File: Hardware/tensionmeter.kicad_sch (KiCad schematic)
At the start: 28 parts, among them IC2 MCP1501T-18E_CHY, U15 L7812, U16 MCP6002-xSN, U24 AD8226BRMZ-R7, U25 AD8226BRMZ-R7

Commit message: Fused 12V
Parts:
- added F7: 300mA, Fuse:Fuse_0603_1608Metric_Pad1.05x0.95mm_HandSolder, symbol Device:Polyfuse_Small
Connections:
- net +12V: now also F7.2; no longer C72.1, U15.3 (OUT)
- new net: C72.1, F7.1, U15.3 (OUT)
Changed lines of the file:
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@@
 	(wire
 		(pts
-			(xy 247.65 64.77) (xy 247.65 67.31)
-		)
-		(stroke
-			(width 0)
-			(type default)
-		)
-	)
-	(wire
-		(pts
 			(xy 114.3 111.76) (xy 132.08 111.76)
 		)
@@
 	(wire
 		(pts
+			(xy 255.27 62.23) (xy 255.27 67.31)
+		)
+		(stroke
+			(width 0)
+			(type default)
+		)
+	)
+	(wire
+		(pts
 			(xy 46.99 96.52) (xy 49.53 96.52)
 		)
@@
 	(wire
 		(pts
+			(xy 255.27 67.31) (xy 251.46 67.31)
+		)
+		(stroke
+			(width 0)
+			(type default)
+		)
+	)
+	(wire
+		(pts
 			(xy 91.44 52.07) (xy 104.14 52.07)
 		)
@@
 	(wire
 		(pts
-			(xy 233.68 77.47) (xy 233.68 74.93)
+			(xy 243.84 67.31) (xy 246.38 67.31)
 		)
 		(stroke
@@
 	(wire
 		(pts
-			(xy 67.31 62.23) (xy 67.31 66.04)
+			(xy 233.68 77.47) (xy 233.68 74.93)
 		)
 		(stroke
@@
 	(wire
 		(pts
-			(xy 142.24 54.61) (xy 163.83 54.61)
+			(xy 67.31 62.23) (xy 67.31 66.04)
 		)
 		(stroke
@@
 	(wire
 		(pts
-			(xy 132.08 101.6) (xy 142.24 101.6)
+			(xy 142.24 54.61) (xy 163.83 54.61)
 		)
 		(stroke
@@
 	(wire
 		(pts
-			(xy 214.63 64.77) (xy 214.63 67.31)
+			(xy 132.08 101.6) (xy 142.24 101.6)
 		)
 		(stroke
@@
 	(wire
 		(pts
-			(xy 31.75 87.63) (xy 31.75 88.9)
+			(xy 214.63 64.77) (xy 214.63 67.31)
 		)
 		(stroke
@@
 	(wire
 		(pts
-			(xy 243.84 67.31) (xy 247.65 67.31)
+			(xy 31.75 87.63) (xy 31.75 88.9)
 		)
 		(stroke
@@
 	)
 	(symbol
+		(lib_id "Device:Polyfuse_Small")
+		(at 248.92 67.31 90)
+		(unit 1)
+		(exclude_from_sim no)
+		(in_bom yes)
+		(on_board yes)
+		(dnp no)
+		(fields_autoplaced yes)
+		(property "Reference" "F7"
+			(at 248.92 62.865 90)
+			(effects
+				(font
+					(size 1.27 1.27)
+				)
+			)
+		)
+		(property "Value" "300mA"
+			(at 248.92 65.405 90)
+			(effects
+				(font
+					(size 1.27 1.27)
+				)
+			)
+		)
+		(property "Footprint" "Fuse:Fuse_0603_1608Metric_Pad1.05x0.95mm_HandSolder"
+			(at 254 66.04 0)
+			(effects
+				(font
+					(size 1.27 1.27)
+				)
+				(justify left)
+				(hide yes)
+			)
+		)
+		(property "Datasheet" "https://www.mouser.pl/datasheet/2/447/YAGO_S_A0011407805_1-2572780.pdf"
+			(at 248.92 67.31 0)
+			(effects
+				(font
+					(size 1.27 1.27)
+				)
+				(hide yes)
+			)
+		)
+		(property "Description" "SMD0603B010TF"
+			(at 248.92 67.31 0)
+			(effects
+				(font
+					(size 1.27 1.27)
+				)
+				(hide yes)
+			)
+		)
+		(property "Mouser Part Number" "603-SMD0603B010TF"
+			(at 248.92 67.31 0)
+			(effects
+				(font
+					(size 1.27 1.27)
+				)
+				(hide yes)
+			)
+		)
+		(pin "1"
+		)
+		(pin "2"
+		)
+		(instances
+			(project "PUTM_EV_Frontbox"
+				(path "/b652b05a-4e3d-4ad1-b032-18886abe7d45/af294f79-0e3a-4ef0-97e3-369c60ae6dab"
+					(reference "F7")
+					(unit 1)
+				)
+			)
+		)
+	)
+	(symbol
 		(lib_id "power:GND")
 		(at 31.75 88.9 0)
@@
 	(symbol
 		(lib_id "power:+12V")
-		(at 247.65 64.77 0)
+		(at 255.27 62.23 0)
 		(unit 1)
 		(exclude_from_sim no)
@@
 		(dnp no)
 		(property "Reference" "#PWR0198"
-			(at 247.65 68.58 0)
+			(at 255.27 66.04 0)
 			(effects
 				(font
@@
 		)
 		(property "Value" "+12V"
-			(at 247.65 59.69 0)
+			(at 255.27 57.15 0)
 			(effects
 				(font
@@
 		)
 		(property "Footprint" ""
-			(at 247.65 64.77 0)
+			(at 255.27 62.23 0)
 			(effects
 				(font
@@
 		)
 		(property "Datasheet" ""
-			(at 247.65 64.77 0)
+			(at 255.27 62.23 0)
 			(effects
 				(font
@@
 		)
 		(property "Description" "Power symbol creates a global label with name \"+12V\""
-			(at 247.65 64.77 0)
+			(at 255.27 62.23 0)
 			(effects
 				(font

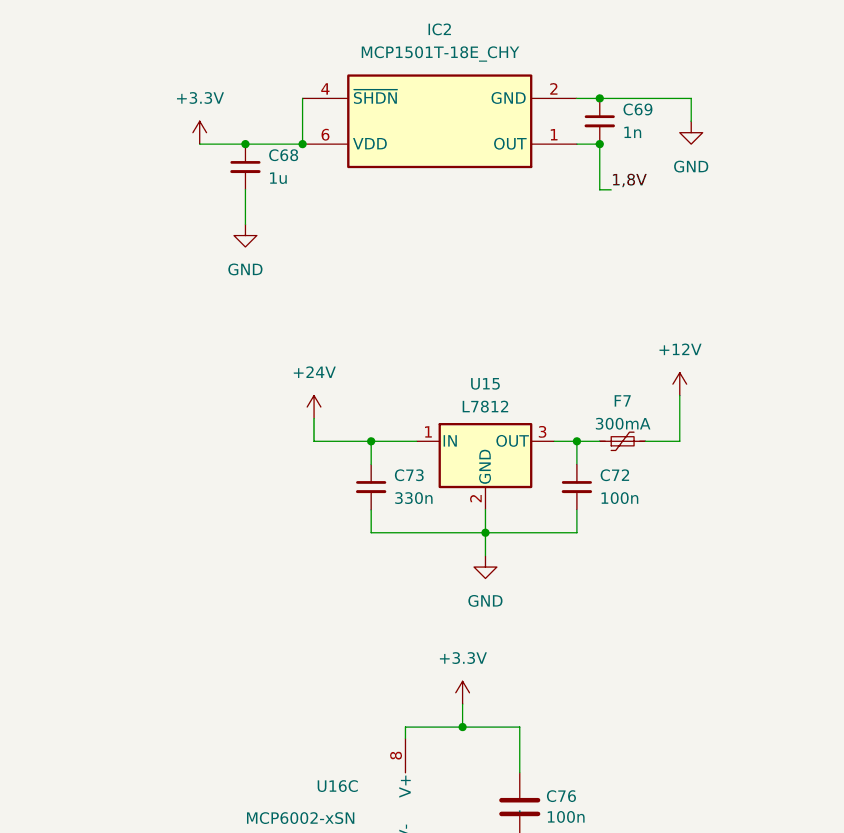
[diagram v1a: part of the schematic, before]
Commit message: Added tensionmeter section, updated APPS resistors for transfer function
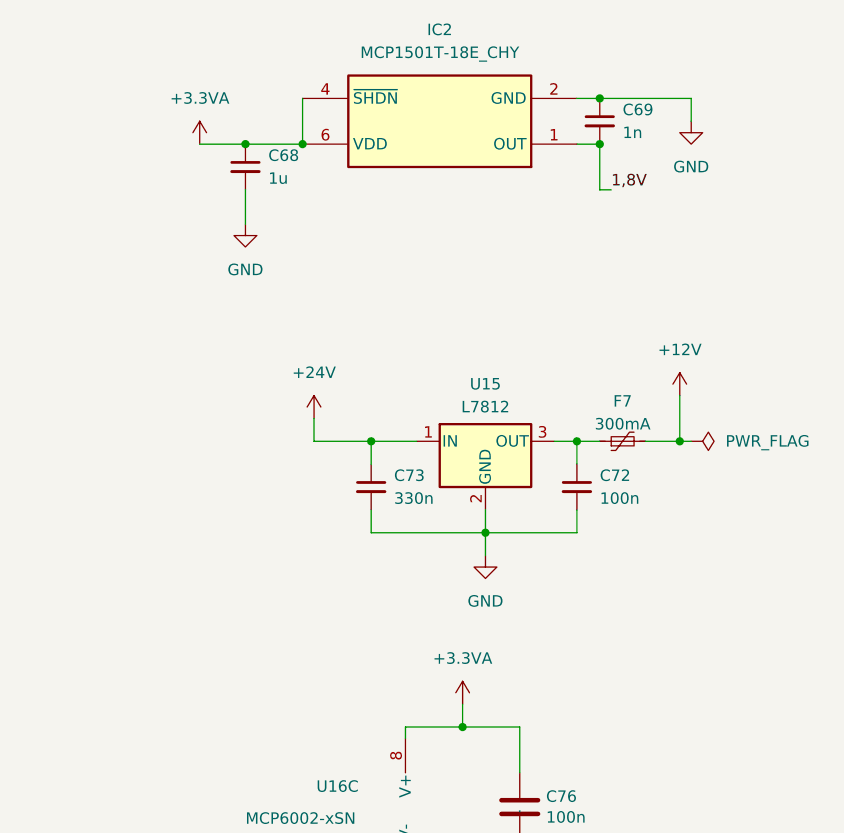
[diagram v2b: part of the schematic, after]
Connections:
- net +3.3V renamed +3.3VA
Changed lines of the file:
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@@
 	)
 	(junction
+		(at 255.27 67.31)
+		(diameter 0)
+		(color 0 0 0 0)
+	)
+	(junction
 		(at 90.17 99.06)
 		(diameter 0)
@@
 	(wire
 		(pts
+			(xy 256.54 67.31) (xy 255.27 67.31)
+		)
+		(stroke
+			(width 0)
+			(type default)
+		)
+	)
+	(wire
+		(pts
 			(xy 46.99 60.96) (xy 49.53 60.96)
 		)
@@
 			)
 		)
-		(property "Value" "+3.3V"
+		(property "Value" "+3.3VA"
 			(at 201.93 29.21 0)
 			(effects
@@
 			)
 		)
-		(property "Value" "+3.3V"
+		(property "Value" "+3.3VA"
 			(at 231.14 91.44 0)
 			(effects
@@
 					(unit 1)
 				)
+			)
+		)
+	)
+	(symbol
+		(lib_id "power:PWR_FLAG")
+		(at 256.54 67.31 270)
+		(unit 1)
+		(exclude_from_sim no)
+		(in_bom yes)
+		(on_board yes)
+		(dnp no)
+		(fields_autoplaced yes)
+		(property "Reference" "#FLG013"
+			(at 258.445 67.31 0)
+			(effects
+				(font
+					(size 1.27 1.27)
+				)
+				(hide yes)
+			)
+		)
+		(property "Value" "PWR_FLAG"
+			(at 260.35 67.3099 90)
+			(effects
+				(font
+					(size 1.27 1.27)
+				)
+				(justify left)
+			)
+		)
+		(property "Footprint" ""
+			(at 256.54 67.31 0)
+			(effects
+				(font
+					(size 1.27 1.27)
+				)
+				(hide yes)
+			)
+		)
+		(property "Datasheet" "~"
+			(at 256.54 67.31 0)
+			(effects
+				(font
+					(size 1.27 1.27)
+				)
+				(hide yes)
+			)
+		)
+		(property "Description" "Special symbol for telling ERC where power comes from"
+			(at 256.54 67.31 0)
+			(effects
+				(font
+					(size 1.27 1.27)
+				)
+				(hide yes)
+			)
+		)
+		(pin "1"
+		)
+		(instances
+			(project ""
+				(path "/b652b05a-4e3d-4ad1-b032-18886abe7d45/af294f79-0e3a-4ef0-97e3-369c60ae6dab"
+					(reference "#FLG013")
+					(unit 1)
+				)

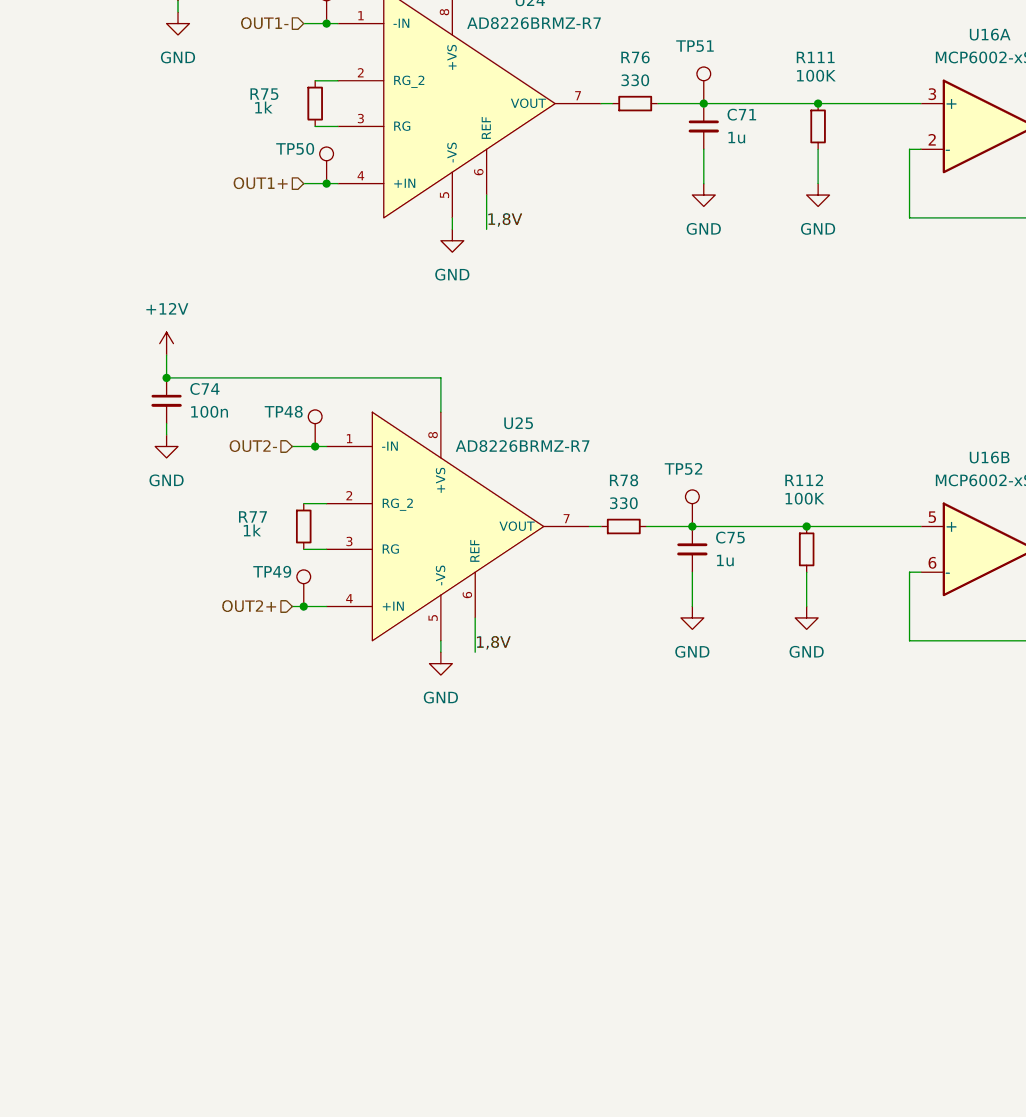
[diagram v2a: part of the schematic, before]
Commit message: Change tensionmeter section for potentiometer uses
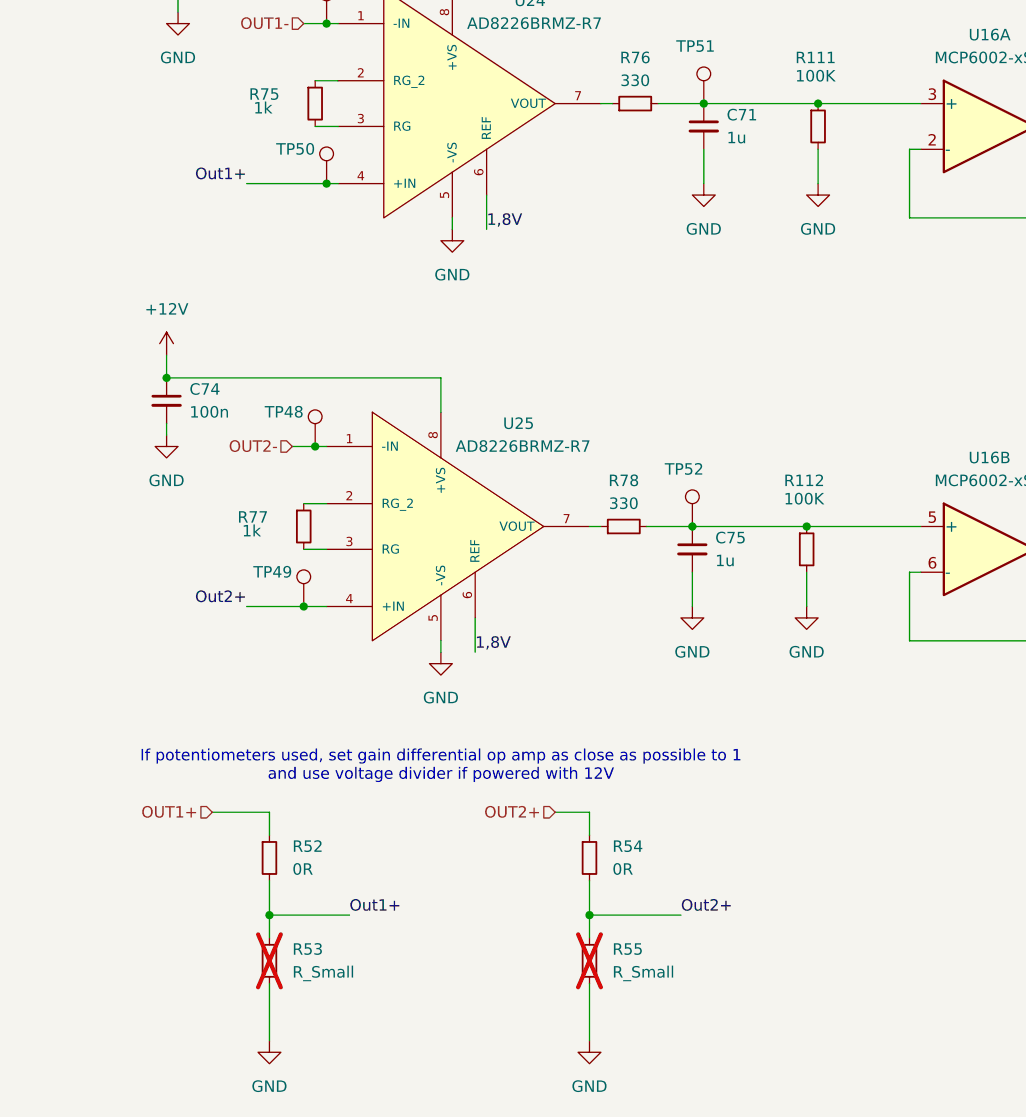
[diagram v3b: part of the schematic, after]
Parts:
- added R52, R54: 0R, Resistor_SMD:R_0603_1608Metric_Pad0.98x0.95mm_HandSolder, symbol Device:R_Small
- added R53, R55: R_Small, Resistor_SMD:R_0603_1608Metric_Pad0.98x0.95mm_HandSolder, symbol Device:R_Small
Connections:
- net GND: now also R53.2, R55.2
- net OUT1+: now also R52.1; no longer TP50.1, U24.4 (+IN)
- net OUT2+: now also R54.1; no longer TP49.1, U25.4 (+IN)
- new net Out1+: R52.2, R53.1, TP50.1, U24.4 (+IN)
- new net Out2+: R54.2, R55.1, TP49.1, U25.4 (+IN)
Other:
- note added: "If potentiometers used, set gain differential op amp as close as possible to 1 and use voltage divider if powered with 12V"

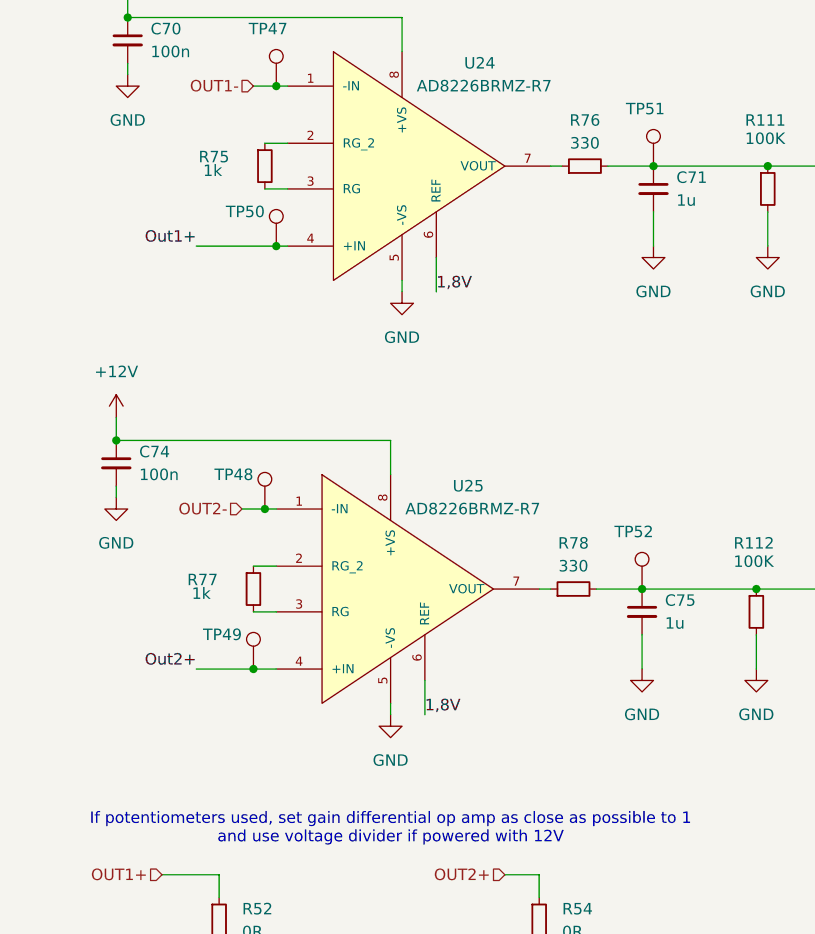
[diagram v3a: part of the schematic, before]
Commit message: Added jumper to differental Op-Amp
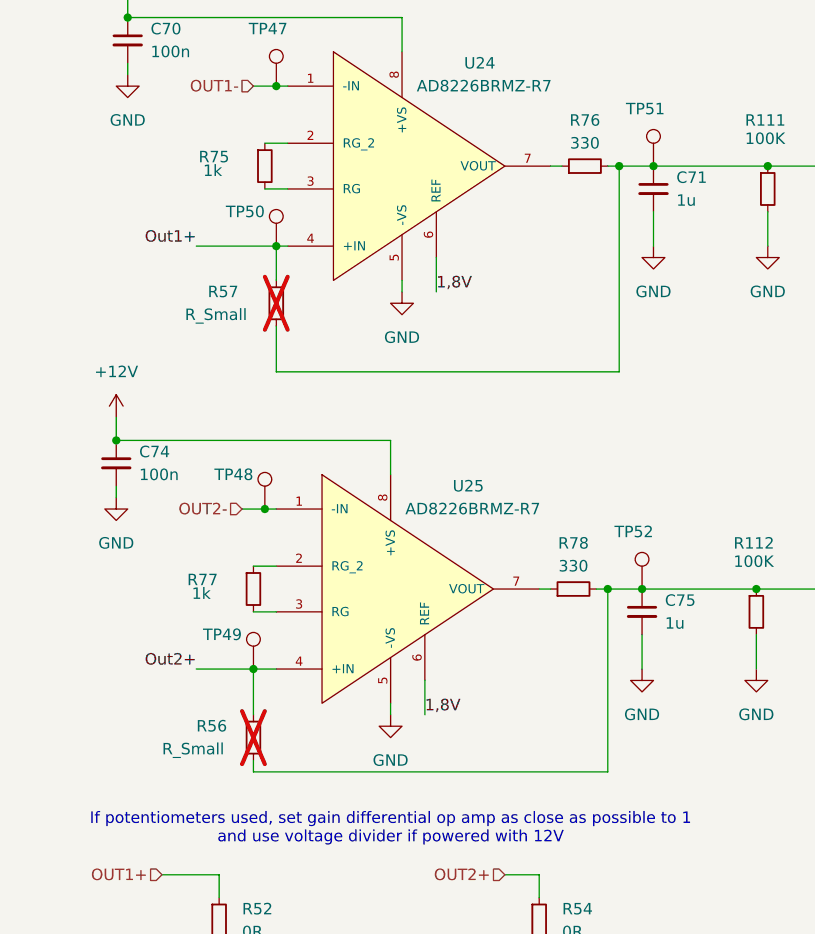
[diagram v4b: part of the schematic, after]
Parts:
- added R56, R57: R_Small, Resistor_SMD:R_0603_1608Metric_Pad0.98x0.95mm_HandSolder, symbol Device:R_Small
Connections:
- net Out1+: now also R57.1
- net Out2+: now also R56.1
- net at C71.1, R111.1, R76.2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: now also R57.2
- net at C75.1, R112.1, R78.2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: now also R56.2
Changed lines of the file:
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@@
 	)
 	(junction
+		(at 86.36 99.06)
+		(diameter 0)
+		(color 0 0 0 0)
+	)
+	(junction
 		(at 49.53 43.18)
 		(diameter 0)
@@
 	)
 	(junction
+		(at 87.63 52.07)
+		(diameter 0)
+		(color 0 0 0 0)
+	)
+	(junction
 		(at 231.14 116.84)
 		(diameter 0)
@@
 	(wire
 		(pts
-			(xy 86.36 52.07) (xy 91.44 52.07)
+			(xy 86.36 52.07) (xy 87.63 52.07)
+		)
+		(stroke
+			(width 0)
+			(type default)
+		)
+	)
+	(wire
+		(pts
+			(xy 86.36 119.38) (xy 86.36 99.06)
 		)
 		(stroke
@@
 	(wire
 		(pts
+			(xy 87.63 52.07) (xy 91.44 52.07)
+		)
+		(stroke
+			(width 0)
+			(type default)
+		)
+	)
+	(wire
+		(pts
 			(xy 33.02 33.02) (xy 33.02 35.56)
 		)
@@
 	(wire
 		(pts
+			(xy 49.53 60.96) (xy 49.53 64.77)
+		)
+		(stroke
+			(width 0)
+			(type default)
+		)
+	)
+	(wire
+		(pts
 			(xy 90.17 99.06) (xy 102.87 99.06)
 		)
@@
 	(wire
 		(pts
+			(xy 49.53 74.93) (xy 87.63 74.93)
+		)
+		(stroke
+			(width 0)
+			(type default)
+		)
+	)
+	(wire
+		(pts
 			(xy 243.84 67.31) (xy 243.84 69.85)
 		)
@@
 	(wire
 		(pts
+			(xy 46.99 107.95) (xy 46.99 113.03)
+		)
+		(stroke
+			(width 0)
+			(type default)
+		)
+	)
+	(wire
+		(pts
 			(xy 231.14 119.38) (xy 231.14 116.84)
 		)
@@
 	(wire
 		(pts
+			(xy 87.63 52.07) (xy 87.63 74.93)
+		)
+		(stroke
+			(width 0)
+			(type default)
+		)
+	)
+	(wire
+		(pts
 			(xy 256.54 31.75) (xy 256.54 29.21)
 		)
@@
 	(wire
 		(pts
+			(xy 86.36 99.06) (xy 90.17 99.06)
+		)
+		(stroke
+			(width 0)
+			(type default)
+		)
+	)
+	(wire
+		(pts
 			(xy 114.3 64.77) (xy 132.08 64.77)
 		)
@@
 	(wire
 		(pts
-			(xy 85.09 99.06) (xy 90.17 99.06)
+			(xy 85.09 99.06) (xy 86.36 99.06)
 		)
 		(stroke
@@
 	(wire
 		(pts
+			(xy 46.99 119.38) (xy 86.36 119.38)
+		)
+		(stroke
+			(width 0)
+			(type default)
+		)
+	)
+	(wire
+		(pts
 			(xy 102.87 104.14) (xy 102.87 107.95)
 		)
@@
 	(wire
 		(pts
+			(xy 46.99 119.38) (xy 46.99 118.11)
+		)
+		(stroke
+			(width 0)
+			(type default)
+		)
+	)
+	(wire
+		(pts
 			(xy 224.79 99.06) (xy 224.79 100.33)
 		)
@@
 	(wire
 		(pts
+			(xy 49.53 69.85) (xy 49.53 74.93)
+		)
+		(stroke
+			(width 0)
+			(type default)
+		)
+	)
+	(wire
+		(pts
 			(xy 247.65 39.37) (xy 246.38 39.37)
 		)
@@
 	)
 	(symbol
+		(lib_id "Device:R_Small")
+		(at 46.99 115.57 0)
+		(unit 1)
+		(exclude_from_sim no)
+		(in_bom yes)
+		(on_board yes)
+		(dnp yes)
+		(property "Reference" "R56"
+			(at 40.64 114.3 0)
+			(effects
+				(font
+					(size 1.27 1.27)
+				)
+				(justify left)
+			)
+		)
+		(property "Value" "R_Small"
+			(at 36.83 116.84 0)
+			(effects
+				(font
+					(size 1.27 1.27)
+				)
+				(justify left)
+			)
+		)
+		(property "Footprint" "Resistor_SMD:R_0603_1608Metric_Pad0.98x0.95mm_HandSolder"
+			(at 46.99 115.57 0)
+			(effects
+				(font
+					(size 1.27 1.27)
+				)
+				(hide yes)
+			)
+		)
+		(property "Datasheet" "~"
+			(at 46.99 115.57 0)
+			(effects
+				(font
+					(size 1.27 1.27)
+				)
+				(hide yes)
+			)
+		)
+		(property "Description" "Resistor, small symbol"
+			(at 46.99 115.57 0)
+			(effects
+				(font
+					(size 1.27 1.27)
+				)
+				(hide yes)
+			)
+		)
+		(pin "2"
+		)
+		(pin "1"
+		)
+		(instances
+			(project "PUTM_EV_Frontbox"
+				(path "/b652b05a-4e3d-4ad1-b032-18886abe7d45/af294f79-0e3a-4ef0-97e3-369c60ae6dab"
+					(reference "R56")
+					(unit 1)
+				)
+			)
+		)
+	)
+	(symbol
 		(lib_id "power:GND")
 		(at 233.68 80.01 0)
@@
 					(unit 1)
 				)
+			)
+		)
+	)
+	(symbol
+		(lib_id "Device:R_Small")
+		(at 49.53 67.31 0)
+		(unit 1)
+		(exclude_from_sim no)
+		(in_bom yes)
+		(on_board yes)
+		(dnp yes)
+		(property "Reference" "R57"
+			(at 41.91 66.04 0)
+			(effects
+				(font
+					(size 1.27 1.27)
+				)
+				(justify left)
+			)
+		)
+		(property "Value" "R_Small"
+			(at 39.37 68.58 0)
+			(effects
+				(font
+					(size 1.27 1.27)
+				)
+				(justify left)
+			)
+		)
+		(property "Footprint" "Resistor_SMD:R_0603_1608Metric_Pad0.98x0.95mm_HandSolder"
+			(at 49.53 67.31 0)
+			(effects
+				(font
+					(size 1.27 1.27)
+				)
+				(hide yes)
+			)
+		)
+		(property "Datasheet" "~"
+			(at 49.53 67.31 0)
+			(effects
+				(font
+					(size 1.27 1.27)
+				)
+				(hide yes)
+			)
+		)
+		(property "Description" "Resistor, small symbol"
+			(at 49.53 67.31 0)
+			(effects
+				(font
+					(size 1.27 1.27)
+				)
+				(hide yes)
+			)
+		)
+		(pin "2"
+		)
+		(pin "1"
+		)
+		(instances
+			(project "PUTM_EV_Frontbox"
+				(path "/b652b05a-4e3d-4ad1-b032-18886abe7d45/af294f79-0e3a-4ef0-97e3-369c60ae6dab"
+					(reference "R57")
+					(unit 1)
+				)
